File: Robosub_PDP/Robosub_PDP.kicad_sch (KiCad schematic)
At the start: 7 parts, among them J1 Screw_Terminal_01x10, J2 Screw_Terminal_01x10, J3 Conn_01x02_Pin, J4 Conn_01x02_Pin, J5 Conn_01x02_Pin

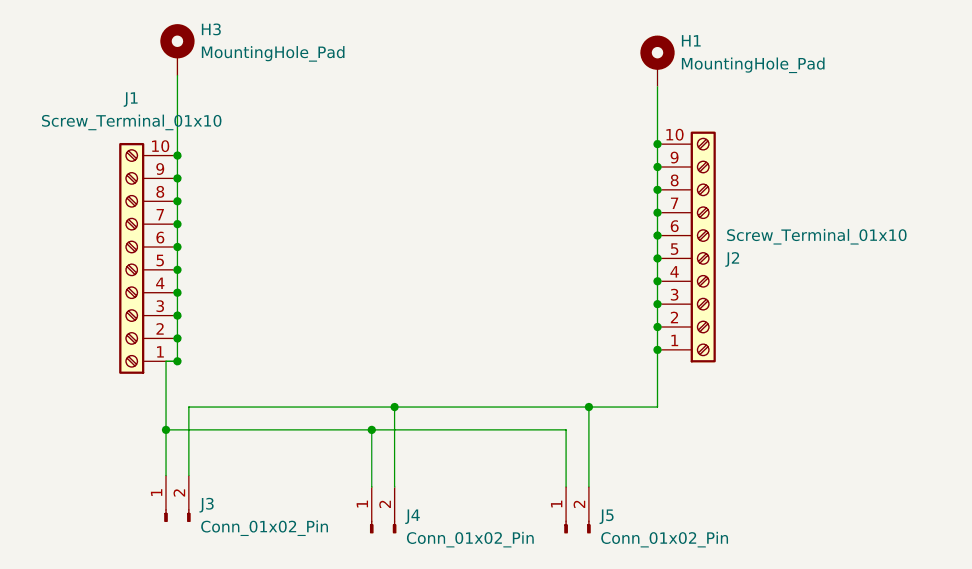
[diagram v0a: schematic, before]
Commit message: edited errors and added logo
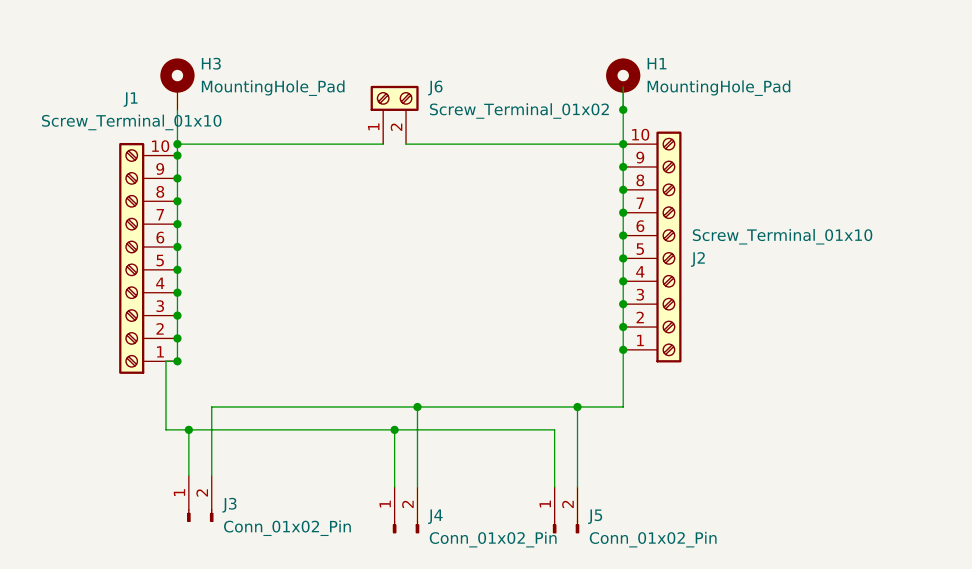
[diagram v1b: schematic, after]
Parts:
- added J6: Screw_Terminal_01x02, TerminalBlock:TerminalBlock_MaiXu_MX126-5.0-02P_1x02_P5.00mm, symbol Connector:Screw_Terminal_01x02
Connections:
- net at H3.1, J1.1 (Pin_1), J1.10 (Pin_10)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: now also J6.1 (Pin_1)
- net at H1.1, J2.1 (Pin_1), J2.10 (Pin_10)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: now also J6.2 (Pin_2)
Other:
- moved on the sheet: H1, H3, J2, J3, J4, J5
